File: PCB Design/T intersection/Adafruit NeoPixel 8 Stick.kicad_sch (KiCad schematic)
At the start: 8 parts, among them CN1 1X4SMT, CN2 1X4SMT, CN3 1X4SMT

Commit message: made microcontroller mount
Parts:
- gave numbers to parts that had none: 1
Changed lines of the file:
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@@
   (symbol (lib_id "LED:WS2812B") (at 106.68 154.94 0) (mirror y) (unit 1)
     (in_bom yes) (on_board yes) (fields_autoplaced)
-    (property "Reference" "D?" (id 0) (at 118.11 150.6093 0))
+    (property "Reference" "D5" (id 0) (at 118.11 150.6093 0))
     (property "Value" "WS2812B" (id 1) (at 118.11 153.1493 0))
     (property "Footprint" "LED_SMD:LED_WS2812B_PLCC4_5.0x5.0mm_P3.2mm" (id 2) (at 105.41 162.56 0)
@@
     )
     (path "/71722173-f4e7-43f3-b269-298e46a2dd46"
-      (reference "D?") (unit 1) (value "WS2812B") (footprint "LED_SMD:LED_WS2812B_PLCC4_5.0x5.0mm_P3.2mm")
-    )
-  )
+      (reference "D5") (unit 1) (value "WS2812B") (footprint "LED_SMD:LED_WS2812B_PLCC4_5.0x5.0mm_P3.2mm")
+    )
+  )

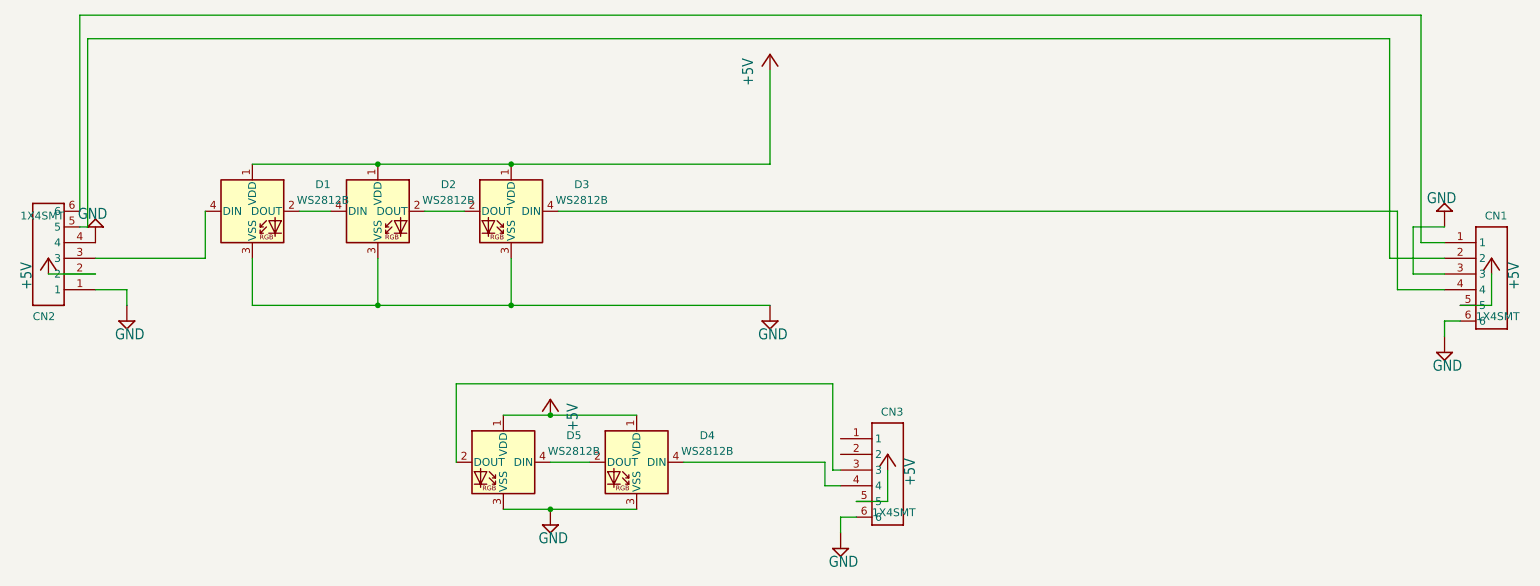
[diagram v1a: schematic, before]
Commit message: left t junction update
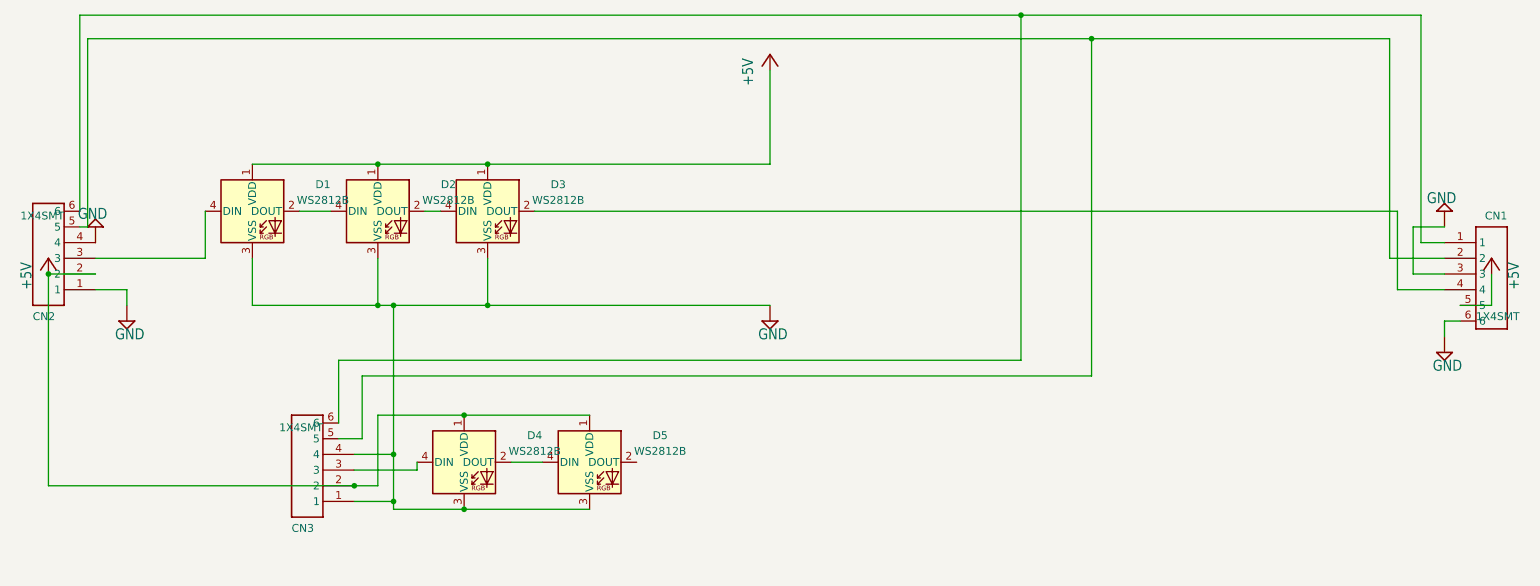
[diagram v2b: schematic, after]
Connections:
- net +5V: now also CN3.2; no longer CN3.5
- net GND: now also CN3.1, CN3.4; no longer CN3.6
- net at D4.4 (DIN): now also CN3.3; no longer CN3.4
- net at D5.2 (DOUT): no longer CN3.3
- net at D2.2 (DOUT): now also D3.4 (DIN); no longer D3.2 (DOUT)
- net at CN1.4: now also D3.2 (DOUT); no longer D3.4 (DIN)
- net at CN1.2, CN2.5: now also CN3.5
- net at CN1.1, CN2.6: now also CN3.6
